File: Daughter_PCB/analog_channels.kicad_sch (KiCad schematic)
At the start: 24 parts, among them J12 Screw_Terminal_01x04, J13 Screw_Terminal_01x02, J14 Conn_01x16, J17 Analog 0, J18 Conn_01x16, U2 AMS1117-3.3, U4 CD74HCT4067QM96Q, U5 OPA607Q1

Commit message: Saving more
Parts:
- removed J12: Screw_Terminal_01x04, TerminalBlock_Phoenix:TerminalBlock_Phoenix_MKDS-1,5-3-5.08_1x03_P5.08mm_Horizontal, symbol Connector:Screw_Terminal_01x03
- removed J13: Screw_Terminal_01x02, TerminalBlock_MetzConnect:TerminalBlock_MetzConnect_Type011_RT05502HBWC_1x02_P5.00mm_Horizontal, symbol Connector:Screw_Terminal_01x02
- removed J14: Conn_01x16, Connector_PinHeader_2.54mm:PinHeader_1x08_P2.54mm_Vertical, symbol Connector_Generic:Conn_01x08
- removed J17: Analog 0, Connector_PinHeader_2.54mm:PinHeader_1x05_P2.54mm_Vertical, symbol Connector_Generic:Conn_01x05
- removed R2: R_Trim, Potentiometer_THT:Potentiometer_Bourns_3296W_Vertical, symbol Device:R_Potentiometer_Trim_US
- removed R5: 100k, Resistor_SMD:R_0603_1608Metric_Pad0.98x0.95mm_HandSolder, symbol Device:R_Small_US
- removed U2: AMS1117-3.3, Package_TO_SOT_SMD:SOT-223-3_TabPin2, symbol Regulator_Linear:AMS1117-3.3
- added J14: Analog 0, Connector_PinHeader_2.54mm:PinHeader_1x05_P2.54mm_Vertical, symbol Connector_Generic:Conn_01x05
- added J15: Screw_Terminal_01x04, TerminalBlock_Phoenix:TerminalBlock_Phoenix_MKDS-1,5-3-5.08_1x03_P5.08mm_Horizontal, symbol Connector:Screw_Terminal_01x03
- added J16: Screw_Terminal_01x02, TerminalBlock_MetzConnect:TerminalBlock_MetzConnect_Type011_RT05502HBWC_1x02_P5.00mm_Horizontal, symbol Connector:Screw_Terminal_01x02
- added J17: Conn_01x08, Connector_PinHeader_2.54mm:PinHeader_1x08_P2.54mm_Vertical, symbol Connector_Generic:Conn_01x08
- added R2: 10k, Resistor_SMD:R_0603_1608Metric_Pad0.98x0.95mm_HandSolder, symbol Device:R_Small_US
- added R5: R_Trim, Potentiometer_THT:Potentiometer_Bourns_3296W_Vertical, symbol Device:R_Potentiometer_Trim_US
- added U3: AMS1117-3.3, Package_TO_SOT_SMD:SOT-223-3_TabPin2, symbol Regulator_Linear:AMS1117-3.3
- J18: value Conn_01x16 -> Conn_01x08
- R3: value 10k -> 100k; now not fitted
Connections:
- net +12V: now also J15.2 (Pin_2), J16.1 (Pin_1), J16.2 (Pin_2)
- net +3.3V: now also U3.2 (VO)
- net +5V: now also J15.3 (Pin_3), U3.3 (VI)
- net AnalogX: now also JP1.1 (A), R3.1, J14.1 (Pin_1), R2.2; no longer JP3.1 (A), R3.2, R6.1
- net GND: now also JP3.1 (A), R6.2, J15.1 (Pin_1), R2.1, R5.3, U3.1 (GND); no longer JP2.1 (A), R3.1
- net MUX_0: now also J14.4 (Pin_4)
- net MUX_1: now also J14.5 (Pin_5)
- net MUX_2: now also J14.3 (Pin_3)
- net MUX_3: now also J14.2 (Pin_2)
- net at C9.1, U5.4 (-): now also R5.2
- net at R1.2, R4.1: now also JP2.2 (B); no longer JP1.2 (B)
- net at JP3.2 (B): now also JP2.1 (A), R4.2, R6.1; no longer R6.2
- net at U4.9 (I0): now also J17.1 (Pin_1)
- net at U4.8 (I1): now also J17.2 (Pin_2)
- net at U4.7 (I2): now also J17.3 (Pin_3)
- net at U4.6 (I3): now also J17.4 (Pin_4)
- net at U4.5 (I4): now also J17.5 (Pin_5)
- net at U4.4 (I5): now also J17.6 (Pin_6)
- net at U4.3 (I6): now also J17.7 (Pin_7)
- net at U4.2 (I7): now also J17.8 (Pin_8)
- new net: JP1.2 (B), R3.2, R5.1

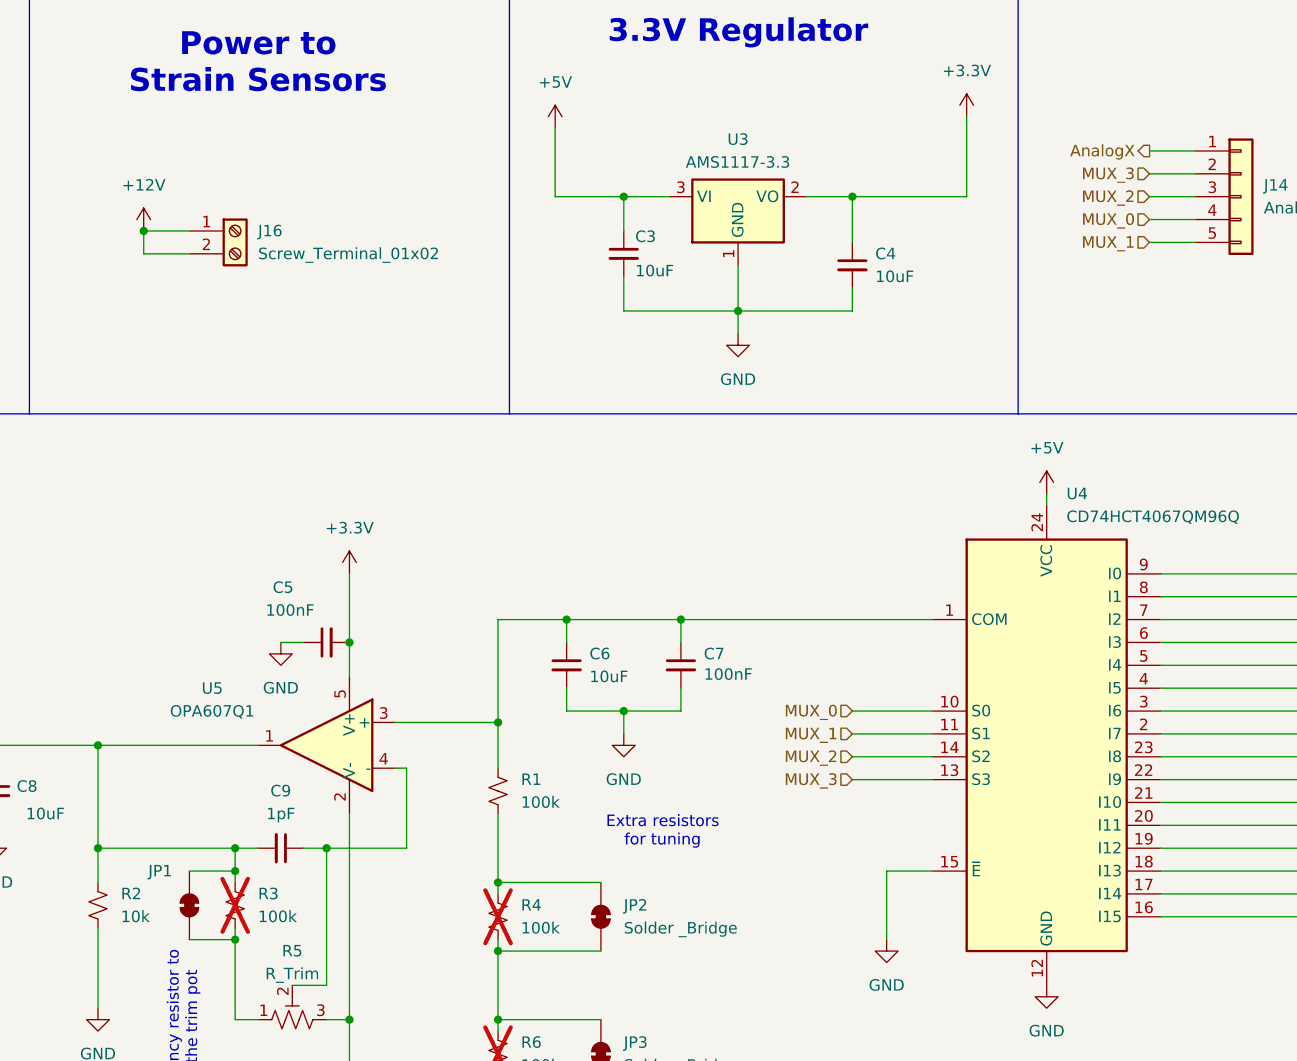
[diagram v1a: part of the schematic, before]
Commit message: Redid the analog multiplexer
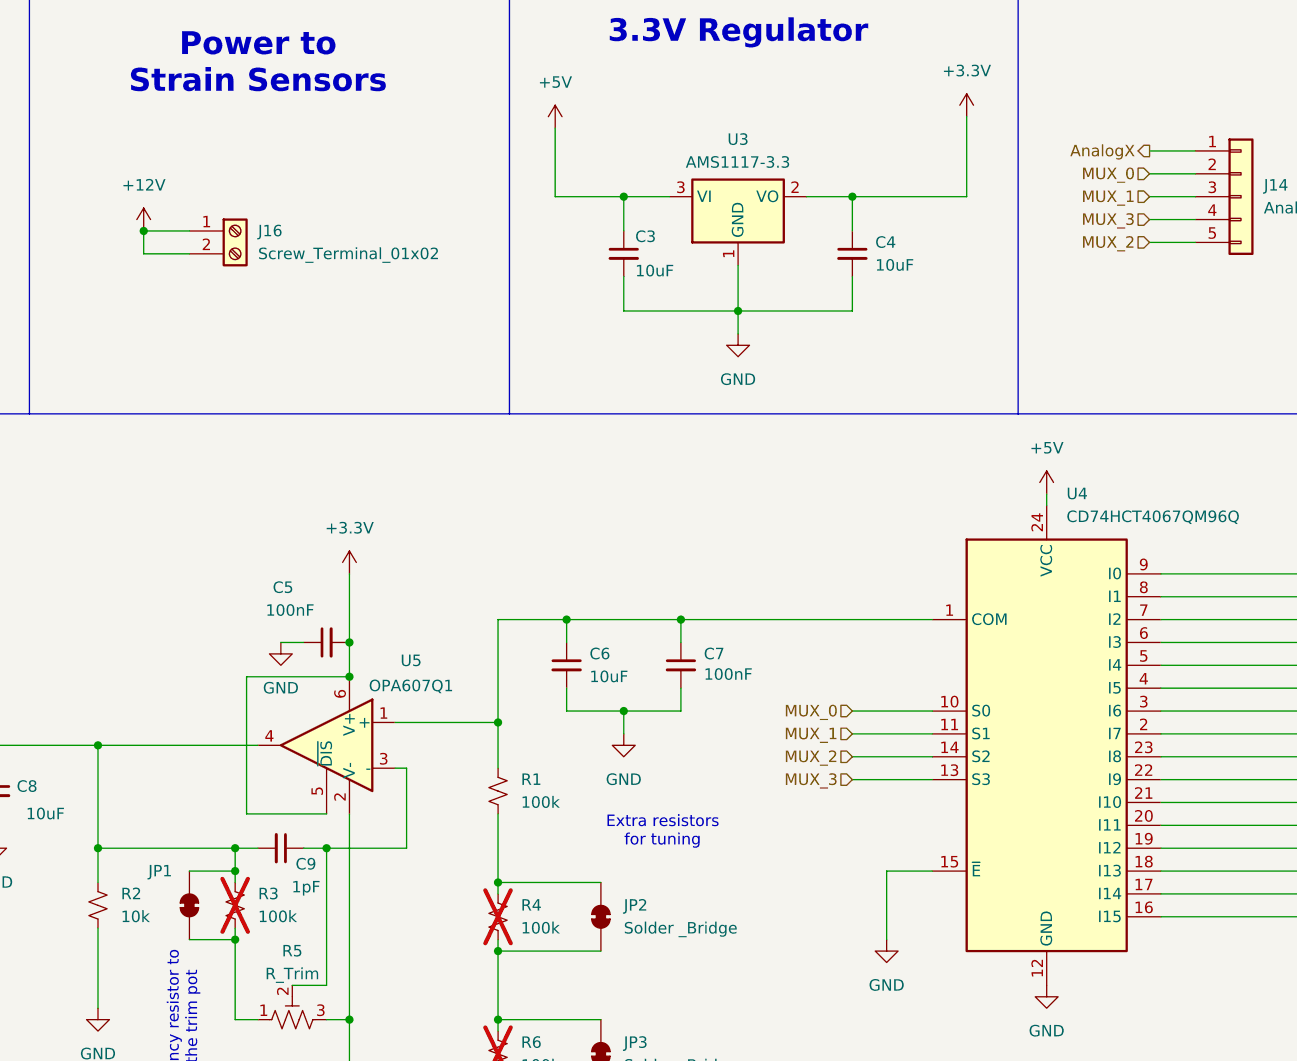
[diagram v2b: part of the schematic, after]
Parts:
- C3, C4: footprint Capacitor_SMD:C_1206_3216Metric -> Capacitor_SMD:C_0805_2012Metric_Pad1.18x1.45mm_HandSolder
- U5: footprint Package_TO_SOT_SMD:TSOT-23-5_HandSoldering -> Package_TO_SOT_SMD:SOT-363_SC-70-6_Handsoldering; symbol Amplifier_Operational:OPA188xxDBV -> Amplifier_Operational:OPA690xDBV
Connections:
- net +3.3V: now also U5.6 (V+)
- net AnalogX: now also U5.4; no longer U5.1
- net MUX_0: now also J14.2 (Pin_2); no longer J14.4 (Pin_4)
- net MUX_1: now also J14.3 (Pin_3); no longer J14.5 (Pin_5)
- net MUX_2: now also J14.5 (Pin_5); no longer J14.3 (Pin_3)
- net MUX_3: now also J14.4 (Pin_4); no longer J14.2 (Pin_2)
- net at C6.1, C7.1, R1.1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: now also U5.1 (+); no longer U5.3 (+)
- net at C9.1, R5.2: now also U5.3 (-); no longer U5.4 (-)
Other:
- moved on the sheet: C4
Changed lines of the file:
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@@
 	)
 	(junction
+		(at 104.14 88.9)
+		(diameter 0)
+		(color 0 0 0 0)
+	)
+	(junction
 		(at 120.65 127)
 		(diameter 0)
@@
 	(wire
 		(pts
-			(xy 160.02 35.56) (xy 160.02 40.64)
+			(xy 160.02 35.56) (xy 160.02 39.37)
 		)
 		(stroke
@@
 	(wire
 		(pts
+			(xy 92.71 88.9) (xy 92.71 104.14)
+		)
+		(stroke
+			(width 0)
+			(type default)
+		)
+	)
+	(wire
+		(pts
 			(xy 120.65 82.55) (xy 128.27 82.55)
 		)
@@
 	(wire
 		(pts
-			(xy 160.02 48.26) (xy 160.02 45.72)
+			(xy 160.02 48.26) (xy 160.02 44.45)
 		)
 		(stroke
@@
 	(wire
 		(pts
+			(xy 92.71 104.14) (xy 101.6 104.14)
+		)
+		(stroke
+			(width 0)
+			(type default)
+		)
+	)
+	(wire
+		(pts
 			(xy 194.31 113.03) (xy 219.71 113.03)
 		)
@@
 	(wire
 		(pts
+			(xy 104.14 88.9) (xy 92.71 88.9)
+		)
+		(stroke
+			(width 0)
+			(type default)
+		)
+	)
+	(wire
+		(pts
 			(xy 110.49 99.06) (xy 110.49 107.95)
 		)
@@
 	(hierarchical_label "MUX_3"
 		(shape input)
-		(at 193.04 33.02 180)
+		(at 193.04 38.1 180)
 		(effects
 			(font
@@
 	(hierarchical_label "MUX_0"
 		(shape input)
-		(at 193.04 38.1 180)
+		(at 193.04 33.02 180)
 		(effects
 			(font
@@
 	(hierarchical_label "MUX_1"
 		(shape input)
-		(at 193.04 40.64 180)
+		(at 193.04 35.56 180)
 		(effects
 			(font
@@
 	(hierarchical_label "MUX_2"
 		(shape input)
-		(at 193.04 35.56 180)
+		(at 193.04 40.64 180)
 		(effects
 			(font
@@
 			)
 		)
-		(property "Footprint" "Capacitor_SMD:C_1206_3216Metric"
+		(property "Footprint" "Capacitor_SMD:C_0805_2012Metric_Pad1.18x1.45mm_HandSolder"
 			(at 134.62 41.91 0)
 			(effects
@@
 		(dnp no)
 		(property "Reference" "C9"
-			(at 96.5137 101.6 90)
+			(at 99.314 109.728 90)
 			(effects
 				(font
@@
 		)
 		(property "Value" "1pF"
-			(at 96.5137 104.14 90)
+			(at 99.314 112.268 90)
 			(effects
 				(font
@@
 	)
 	(symbol
-		(lib_id "Amplifier_Operational:OPA188xxDBV")
+		(lib_id "Amplifier_Operational:OPA690xDBV")
 		(at 101.6 96.52 0)
 		(mirror y)
@@
 		(dnp no)
 		(property "Reference" "U5"
-			(at 88.9 90.2014 0)
+			(at 110.998 87.122 0)
 			(effects
 				(font
@@
 		)
 		(property "Value" "OPA607Q1"
-			(at 88.9 92.7414 0)
+			(at 110.998 89.916 0)
 			(effects
 				(font
@@
 			)
 		)
-		(property "Footprint" "Package_TO_SOT_SMD:TSOT-23-5_HandSoldering"
+		(property "Footprint" "Package_TO_SOT_SMD:SOT-363_SC-70-6_Handsoldering"
 			(at 101.6 96.52 0)
 			(effects
@@
 			)
 		)
-		(property "Datasheet" "https://www.ti.com/lit/ds/symlink/opa607-q1.pdf?ts=1737552136542&ref_url=https%253A%252F%252Flv.mouser.com%252F"
+		(property "Datasheet" "https://www.ti.com/lit/ds/symlink/opa690.pdf"
 			(at 101.6 91.44 0)
 			(effects
@@
 			)
 		)
-		(property "Description" "Automotive, 50-MHz , Rail to Rail Output CMOS Operational Amplifier"
+		(property "Description" "Single Low-Power, 500 MHz GBW, ±2.5V to ±5V Dual Supply, 5V to 12V Single Supply, 190mA output current, 1.8kV/us slew rate, Voltage-Feedback Operational Amplifier with Disable, SOT-23-6"
 			(at 101.6 96.52 0)
 			(effects
@@
 		(pin "4"
 		)
+		(pin "6"
+		)
 		(instances
 			(project "Daughter_PCB"
@@
 	(symbol
 		(lib_id "Device:C_Small")
-		(at 160.02 43.18 0)
+		(at 160.02 41.91 0)
 		(unit 1)
 		(exclude_from_sim no)
@@
 		(fields_autoplaced yes)
 		(property "Reference" "C4"
-			(at 162.56 41.9163 0)
+			(at 162.56 40.6463 0)
 			(effects
 				(font
@@
 		)
 		(property "Value" "10uF"
-			(at 162.56 44.4563 0)
+			(at 162.56 43.1863 0)
 			(effects
 				(font
@@
 			)
 		)
-		(property "Footprint" "Capacitor_SMD:C_1206_3216Metric"
-			(at 160.02 43.18 0)
+		(property "Footprint" "Capacitor_SMD:C_0805_2012Metric_Pad1.18x1.45mm_HandSolder"
+			(at 160.02 41.91 0)
 			(effects
 				(font
@@
 		)
 		(property "Datasheet" "~"
-			(at 160.02 43.18 0)
+			(at 160.02 41.91 0)
 			(effects
 				(font
@@
 		)
 		(property "Description" ""
-			(at 160.02 43.18 0)
+			(at 160.02 41.91 0)
 			(effects
 				(font
@@
 		)
 		(property "LCSC Part #" "C13585"
-			(at 160.02 43.18 0)
+			(at 160.02 41.91 0)
 			(effects
 				(font
@@
 		)
 		(property "JLCPCB Position Offset" ""
-			(at 160.02 43.18 0)
+			(at 160.02 41.91 0)
 			(effects
 				(font
@@
 		)
 		(property "JLCPCB Rotation Offset" ""
-			(at 160.02 43.18 0)
+			(at 160.02 41.91 0)
 			(effects
 				(font
@@
 		)
 		(property "Availability" ""
-			(at 160.02 43.18 0)
+			(at 160.02 41.91 0)
 			(effects
 				(font
@@
 		)
 		(property "Check_prices" ""
-			(at 160.02 43.18 0)
+			(at 160.02 41.91 0)
 			(effects
 				(font
@@
 		)
 		(property "MF" ""
-			(at 160.02 43.18 0)
+			(at 160.02 41.91 0)
 			(effects
 				(font
@@
 		)
 		(property "MP" ""
-			(at 160.02 43.18 0)
+			(at 160.02 41.91 0)
 			(effects
 				(font
@@
 		)
 		(property "Package" ""
-			(at 160.02 43.18 0)
+			(at 160.02 41.91 0)
 			(effects
 				(font
@@
 		)
 		(property "Price" ""
-			(at 160.02 43.18 0)
+			(at 160.02 41.91 0)
 			(effects
 				(font
@@
 		)
 		(property "SnapEDA_Link" ""
-			(at 160.02 43.18 0)
+			(at 160.02 41.91 0)
 			(effects
 				(font
